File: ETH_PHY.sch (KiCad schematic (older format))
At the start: 44 parts, among them J4 BELFUSE_0826-1X1T-HS-F, U4 88E1512-XX-NNP2I000, U6 TXS0102DCUR

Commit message: Rename library AMC_FMC_Carrier-PcbDoc-rescue as marble_misc
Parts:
- J4: symbol AMC_FMC_Carrier-PcbDoc-rescue:BELFUSE_0826-1X1T-HS-F-Miscellaneous -> marble_misc:BELFUSE_0826-1X1T-HS-F-Miscellaneous
- OSC1: symbol AMC_FMC_Carrier-PcbDoc-rescue:Oscillator-powerMG-AMC_FMC_Carrier-PcbDoc-rescue -> marble_misc:Oscillator-powerMG-AMC_FMC_Carrier-PcbDoc-rescue
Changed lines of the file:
@@
 RGMII_RX_CLK
 $Comp
-L AMC_FMC_Carrier-PcbDoc-rescue:Oscillator-powerMG-AMC_FMC_Carrier-PcbDoc-rescue OSC1
+L marble_misc:Oscillator-powerMG-AMC_FMC_Carrier-PcbDoc-rescue OSC1
 U 1 1 5C76AE78
 P 4600 3400
@@
 	3050 1500 3250 1500
 $Comp
-L AMC_FMC_Carrier-PcbDoc-rescue:BELFUSE_0826-1X1T-HS-F-Miscellaneous J4
+L marble_misc:BELFUSE_0826-1X1T-HS-F-Miscellaneous J4
 U 1 1 5DB81DF6
 P 12500 1900
@@
 Connection ~ 14500 4500
 $Comp
-L AMC_FMC_Carrier-PcbDoc-rescue:power_PWR_FLAG-AMC_FMC_Carrier-PcbDoc-cache #FLG0103
+L marble_misc:power_PWR_FLAG-AMC_FMC_Carrier-PcbDoc-cache #FLG0103
 U 1 1 5D15ABC3
 P 5250 6650
@@
 $EndComp
 $Comp
-L AMC_FMC_Carrier-PcbDoc-rescue:power_PWR_FLAG-AMC_FMC_Carrier-PcbDoc-cache #FLG0104
+L marble_misc:power_PWR_FLAG-AMC_FMC_Carrier-PcbDoc-cache #FLG0104
 U 1 1 5D15B1F6
 P 5250 7600
@@
 $EndComp
 $Comp
-L AMC_FMC_Carrier-PcbDoc-rescue:power_PWR_FLAG-AMC_FMC_Carrier-PcbDoc-cache #FLG0105
+L marble_misc:power_PWR_FLAG-AMC_FMC_Carrier-PcbDoc-cache #FLG0105
 U 1 1 5D15B45E
 P 14500 2000

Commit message: Strip extraneous AMC_FMC_Carrier-PcbDoc-rescue and powerMG from symbol names
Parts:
- OSC1: symbol marble_misc:Oscillator-powerMG-AMC_FMC_Carrier-PcbDoc-rescue -> marble_misc:Oscillator
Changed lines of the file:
@@
 RGMII_RX_CLK
 $Comp
-L marble_misc:Oscillator-powerMG-AMC_FMC_Carrier-PcbDoc-rescue OSC1
+L marble_misc:Oscillator OSC1
 U 1 1 5C76AE78
 P 4600 3400

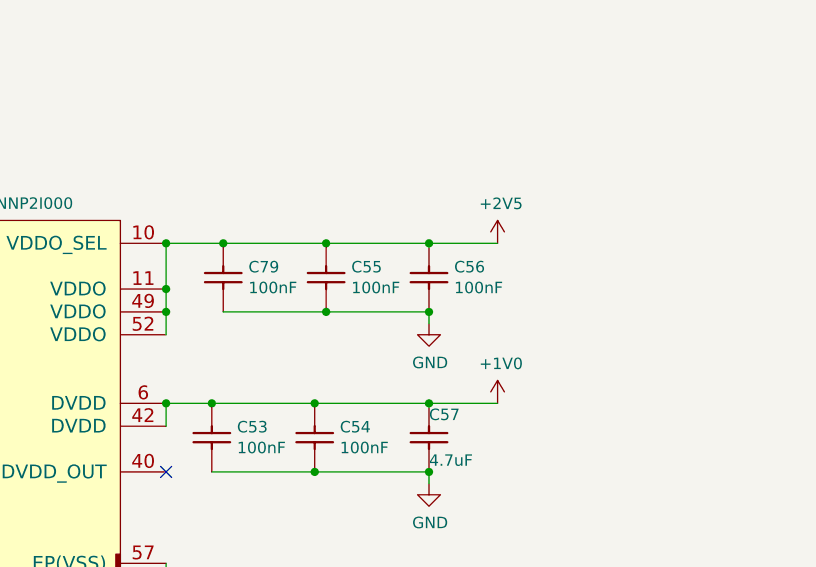
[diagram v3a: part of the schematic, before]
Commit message: tie U4 (88E1512 Ethernet PHY): VDDO_SEL (10) low for VDDO = 2.5V
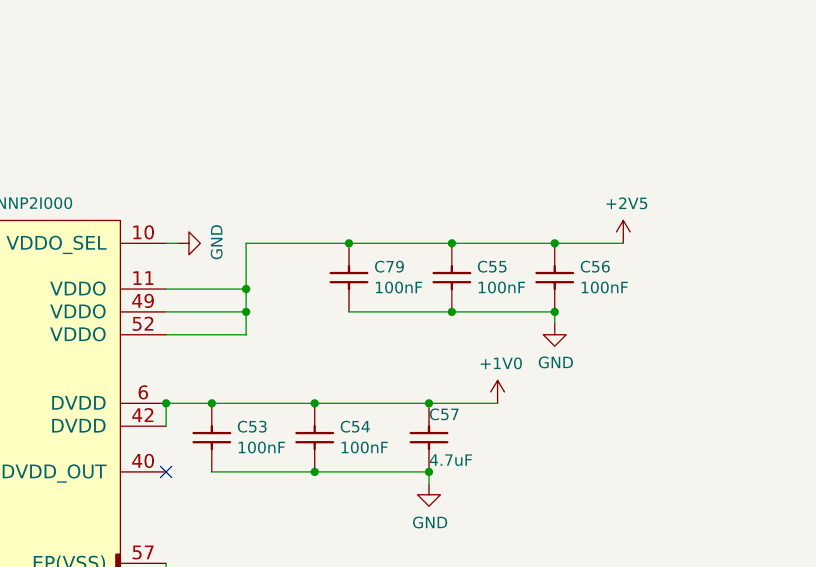
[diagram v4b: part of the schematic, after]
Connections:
- wire segments 163 -> 167
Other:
- moved on the sheet: C55, C56, C79

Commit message: Convert all footprints to use Marble nickname
Includes both .sch and .lib files
Includes both bare footprint names and those with CERN-like nicknames
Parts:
- C352, C41, C43, C44, C45, C46, C48, C49, C50, C51, C52, C53, C54, C55, C56, C58, C59, C60, C79: footprint CAPC0603X33N -> Marble:CAPC0603X33N
- C374, C375: footprint CAPC1005X55N -> Marble:CAPC1005X55N
- C42, C47: footprint CAPC1608X87N -> Marble:CAPC1608X87N
- C57: footprint CAPC1709X95N -> Marble:CAPC1709X95N
- J4: footprint BELFUSE_0826-1X1T-80-F -> Marble:BELFUSE_0826-1X1T-80-F
- L3, L4: footprint INDC1608X65N -> Marble:INDC1608X65N
- OSC1: footprint ICs And Semiconductors SMD:OSC_MICREL_2520 -> Marble:OSC_MICREL_2520
- R156, R165, R262, R291, R292, R293, R294, R295, R296, R65, R67: footprint RESC1005X40N -> Marble:RESC1005X40N
- R62, R64, R66: footprint RESC1608X55N -> Marble:RESC1608X55N
- U4: footprint ICs And Semiconductors SMD:QFN50P800X800X100-57N-S437 -> Marble:QFN50P800X800X100-57N-S437
- U6: footprint SOP50P310X90-8N -> Marble:SOP50P310X90-8N

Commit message: Get rid of "~" attribute in instances
This makes instances line up better with our library
Use a very short python program to rename "~" to "Val" and remove the old "Val".
Required a little pre-patch to correctly handle R297 R298 R299 R300 R162 R274 R197 R198, which had no "~" field.
No net changes to "Val" field contents.
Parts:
- C352, C41, C43, C44, C45, C46, C48, C49, C50, C51, C52, C53, C54, C55, C56, C58, C59, C60, C79: ~ 100nF -> (none)
- C374, C375: ~ 100pF -> (none)
- C42, C47: ~ 10uF -> (none)
- C57: ~ 4.7uF -> (none)
- L3, L4: ~ 120R@100MHz -> (none)
- R156, R67: ~ 240 -> (none)
- R165, R65: ~ 0 -> (none)
- R262: ~ 10k -> (none)
- R291, R292, R293, R294, R295, R296: ~ 22 -> (none)
- R62, R64, R66: ~ 4k99 -> (none)
